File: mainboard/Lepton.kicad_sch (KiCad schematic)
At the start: 17 parts, among them IC1001 TXB0104RUT, IC1002 PCA9306JK, IC1003 TXB0104RUT, X1001 LEPTON, Y1001 25 MHz

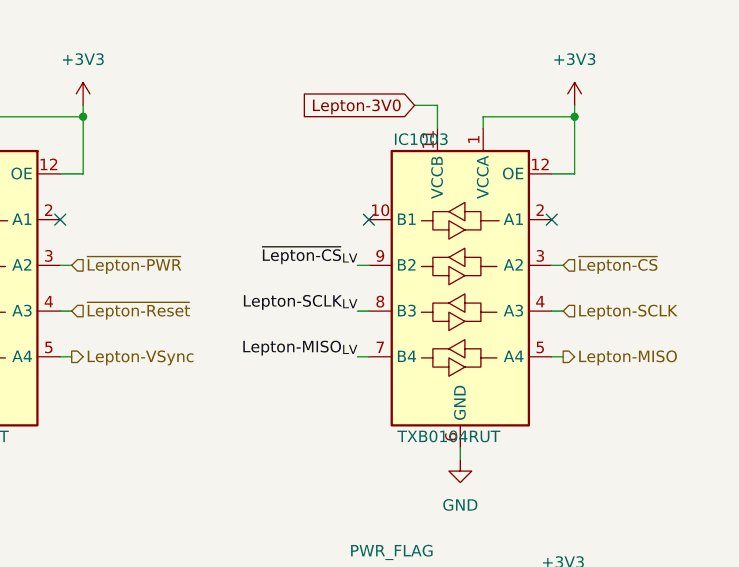
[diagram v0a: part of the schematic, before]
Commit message: Continue routing, add flash LEDs for the RGB camera, add PWM controller for the Display Backlight and the flash LEDs, add Polyfuse for the battery
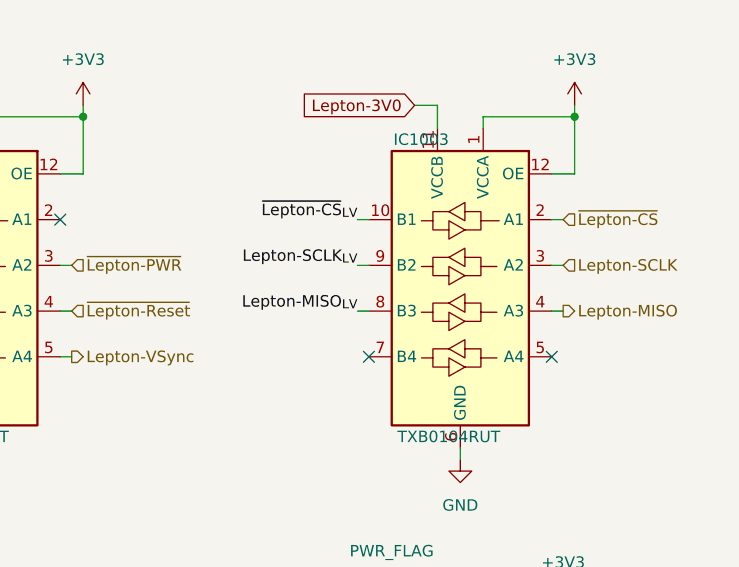
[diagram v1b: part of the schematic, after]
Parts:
- R1004, R1005, R1007, R1008: mouser# (none) -> 603-RC0603FR-073K3L
- R1006: mouser# (none) -> 603-RC0603FR-07200KL
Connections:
- net Lepton-MISO: now also IC1003.4 (A3); no longer IC1003.5 (A4)
- net Lepton-MISO_{LV}: now also IC1003.8 (B3); no longer IC1003.7 (B4)
- net Lepton-SCLK: now also IC1003.3 (A2); no longer IC1003.4 (A3)
- net Lepton-SCLK_{LV}: now also IC1003.9 (B2); no longer IC1003.8 (B3)
- net ~{Lepton-CS}: now also IC1003.2 (A1); no longer IC1003.3 (A2)
- net ~{Lepton-CS}_{LV}: now also IC1003.10 (B1); no longer IC1003.9 (B2)
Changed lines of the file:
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@@
 	)
 	(no_connect
+		(at 245.11 81.28)
+	)
+	(no_connect
 		(at 72.39 83.82)
 	)
 	(no_connect
-		(at 72.39 68.58)
+		(at 265.43 81.28)
 	)
 	(no_connect
-		(at 190.5 66.04)
+		(at 72.39 68.58)
 	)
 	(no_connect
-		(at 265.43 66.04)
+		(at 190.5 66.04)
 	)
 	(no_connect
@@
 		(at 85.09 50.8)
 	)
-	(no_connect
-		(at 245.11 66.04)
-	)
 	(wire
 		(pts
@@
 	(wire
 		(pts
-			(xy 265.43 81.28) (xy 266.7 81.28)
-		)
-		(stroke
-			(width 0)
-			(type default)
-		)
-	)
-	(wire
-		(pts
 			(xy 267.97 60.96) (xy 265.43 60.96)
 		)
@@
 	(wire
 		(pts
+			(xy 265.43 66.04) (xy 266.7 66.04)
+		)
+		(stroke
+			(width 0)
+			(type default)
+		)
+	)
+	(wire
+		(pts
 			(xy 203.2 54.61) (xy 203.2 55.88)
 		)
@@
 	(wire
 		(pts
-			(xy 96.52 76.2) (xy 85.09 76.2)
+			(xy 243.84 66.04) (xy 245.11 66.04)
 		)
 		(stroke
@@
 	(wire
 		(pts
-			(xy 242.57 121.92) (xy 245.11 121.92)
+			(xy 96.52 76.2) (xy 85.09 76.2)
 		)
 		(stroke
@@
 	(wire
 		(pts
-			(xy 71.12 81.28) (xy 71.12 88.9)
+			(xy 242.57 121.92) (xy 245.11 121.92)
 		)
 		(stroke
@@
 	(wire
 		(pts
-			(xy 265.43 137.16) (xy 271.78 137.16)
+			(xy 71.12 81.28) (xy 71.12 88.9)
 		)
 		(stroke
@@
 	(wire
 		(pts
-			(xy 85.09 53.34) (xy 86.36 53.34)
+			(xy 265.43 137.16) (xy 271.78 137.16)
 		)
 		(stroke
@@
 	(wire
 		(pts
-			(xy 54.61 76.2) (xy 57.15 76.2)
+			(xy 85.09 53.34) (xy 86.36 53.34)
 		)
 		(stroke
@@
 	(wire
 		(pts
-			(xy 85.09 73.66) (xy 97.79 73.66)
+			(xy 54.61 76.2) (xy 57.15 76.2)
 		)
 		(stroke
@@
 	(wire
 		(pts
-			(xy 243.84 81.28) (xy 245.11 81.28)
+			(xy 85.09 73.66) (xy 97.79 73.66)
 		)
 		(stroke
@@
 	)
 	(label "~{Lepton-CS}_{LV}"
-		(at 243.84 71.12 180)
+		(at 243.84 66.04 180)
 		(effects
 			(font
@@
 	)
 	(label "Lepton-MISO_{LV}"
-		(at 243.84 81.28 180)
+		(at 243.84 76.2 180)
 		(effects
 			(font
@@
 	)
 	(label "Lepton-SCLK_{LV}"
-		(at 243.84 76.2 180)
+		(at 243.84 71.12 180)
 		(effects
 			(font
@@
 	(hierarchical_label "~{Lepton-CS}"
 		(shape input)
-		(at 266.7 71.12 0)
+		(at 266.7 66.04 0)
 		(effects
 			(font
@@
 	(hierarchical_label "Lepton-MISO"
 		(shape output)
-		(at 266.7 81.28 0)
+		(at 266.7 76.2 0)
 		(effects
 			(font
@@
 	(hierarchical_label "Lepton-SCLK"
 		(shape input)
-		(at 266.7 76.2 0)
+		(at 266.7 71.12 0)
 		(effects
 			(font
@@
 			)
 		)
-		(property "Datasheet" "~"
+		(property "Datasheet" "https://www.mouser.com/catalog/specsheets/YAGEO_PYu_RC_Group_51_RoHS_L_12.pdf"
 			(at 265.43 128.27 0)
 			(effects
@@
 			)
 		)
-		(property "mouser#" ""
+		(property "mouser#" "603-RC0603FR-073K3L"
 			(at 265.43 128.27 0)
 			(effects
@@
 			)
 		)
-		(property "Datasheet" "~"
+		(property "Datasheet" "https://www.mouser.com/catalog/specsheets/YAGEO_PYu_RC_Group_51_RoHS_L_12.pdf"
 			(at 257.81 114.3 0)
 			(effects
@@
 			)
 		)
-		(property "mouser#" ""
+		(property "mouser#" "603-RC0603FR-07200KL"
 			(at 257.81 114.3 0)
 			(effects
@@
 			)
 		)
-		(property "Datasheet" "~"
+		(property "Datasheet" "https://www.mouser.com/catalog/specsheets/YAGEO_PYu_RC_Group_51_RoHS_L_12.pdf"
 			(at 267.97 128.27 0)
 			(effects
@@
 			)
 		)
-		(property "mouser#" ""
+		(property "mouser#" "603-RC0603FR-073K3L"
 			(at 267.97 128.27 0)
 			(effects
@@
 			)
 		)
-		(property "Datasheet" "~"
+		(property "Datasheet" "https://www.mouser.com/catalog/specsheets/YAGEO_PYu_RC_Group_51_RoHS_L_12.pdf"
 			(at 213.36 128.27 0)
 			(effects
@@
 			)
 		)
-		(property "mouser#" ""
+		(property "mouser#" "603-RC0603FR-073K3L"
 			(at 213.36 128.27 0)
 			(effects
@@
 			)
 		)
-		(property "Datasheet" "~"
+		(property "Datasheet" "https://www.mouser.com/catalog/specsheets/YAGEO_PYu_RC_Group_51_RoHS_L_12.pdf"
 			(at 215.9 128.27 0)
 			(effects
@@
 			)
 		)
-		(property "mouser#" ""
+		(property "mouser#" "603-RC0603FR-073K3L"
 			(at 215.9 128.27 0)
 			(effects

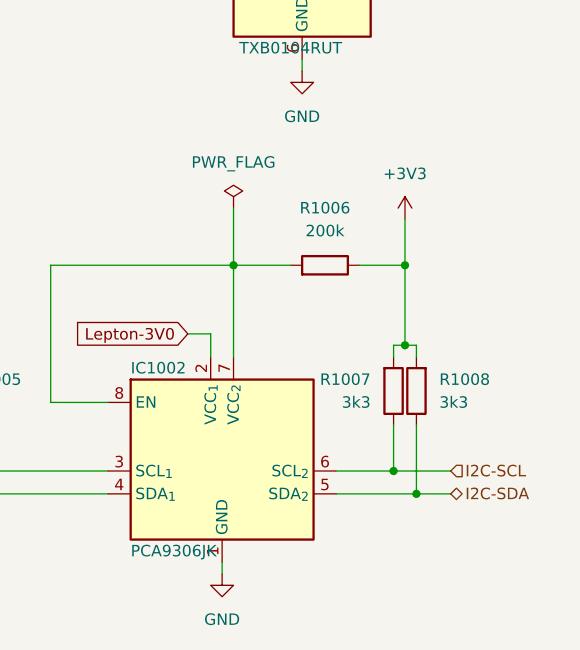
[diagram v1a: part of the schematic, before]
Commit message: New position for display connector
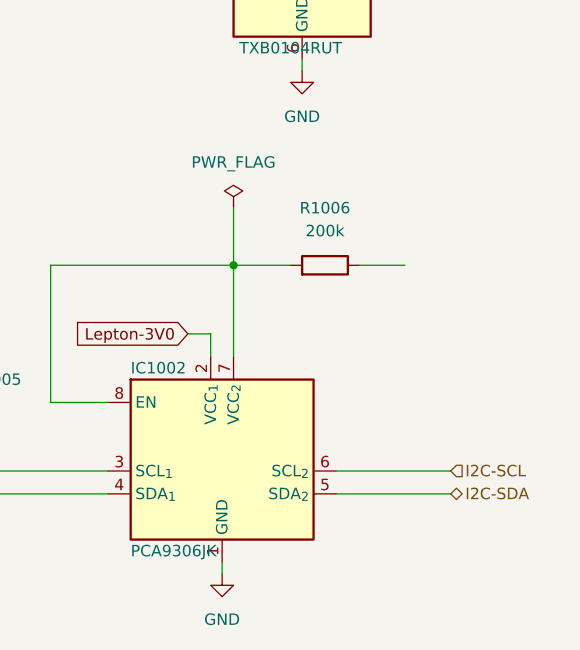
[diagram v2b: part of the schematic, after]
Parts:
- removed R1007, R1008: 3k3, Resistor_SMD:R_0603_1608Metric, symbol Device:R
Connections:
- net +3V3: no longer R1006.1

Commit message: Layout complete
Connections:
- net +3V3: now also R1006.1
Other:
- moved on the sheet: IC1001, IC1002, IC1003, R1001, R1002, R1004, R1005, R1006

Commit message: Task: Issue #7
- Increase the width of the cutout for the temperature sensor
- Add missing component informations
- Fix wrong component informations

Closes: #7

Signed-off-by: Daniel Kampert <DanielKampert@kampis-elektroecke.de>
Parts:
- R1002: mouser# 652-CR0603-J/-000ELF -> 652-CR1206-J/-000ELF
- R1006: manf# RC0603FR-07200KL -> RC0603FR-073K3L
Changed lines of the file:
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@@
 			)
 		)
-		(property "manf#" "RC0603FR-07200KL"
+		(property "manf#" "RC0603FR-073K3L"
 			(at 243.84 102.87 0)
 			(effects
@@
 			)
 		)
-		(property "mouser#" "652-CR0603-J/-000ELF"
+		(property "mouser#" "652-CR1206-J/-000ELF"
 			(at 66.04 82.55 0)
 			(effects

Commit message: Bug: Fixing several component issues
Closes: #17
Closes: #16
Closes: #15
Closes: #14
Closes: #13
Closes: #12

Signed-off-by: Daniel Kampert <danielkampert@kampis-elektroecke.de>
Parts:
- Y1001: manf ASDDV-25.000MHz-LC-T3 -> ABRACON; manf# ABRACON -> ASDDV-25.000MHz-LC-T3
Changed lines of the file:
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@@
 			)
 		)
-		(property "manf" "ASDDV-25.000MHz-LC-T3"
+		(property "manf" "ABRACON"
 			(at 105.41 129.54 0)
 			(effects
@@
 			)
 		)
-		(property "manf#" "ABRACON"
+		(property "manf#" "ASDDV-25.000MHz-LC-T3"
 			(at 105.41 129.54 0)
 			(effects

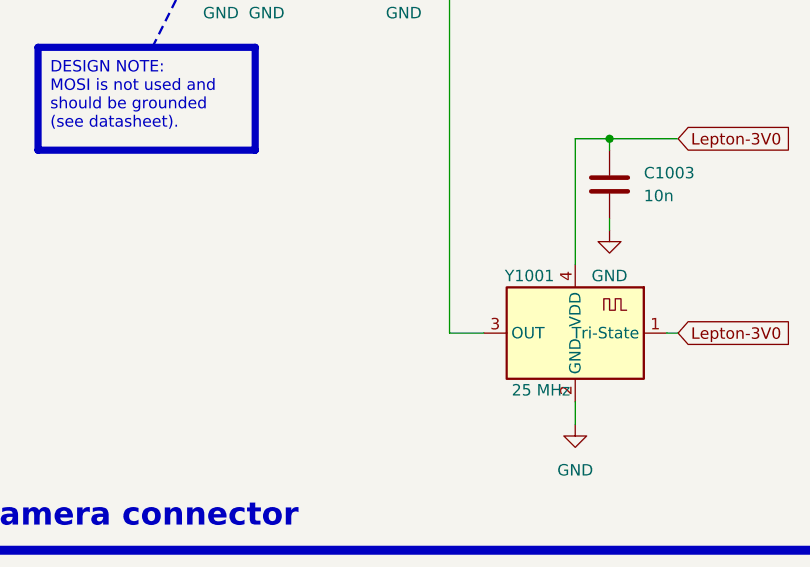
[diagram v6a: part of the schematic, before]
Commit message: Changed: Fix different minor assembly ToDos
Signed-off-by: Daniel Kampert <DanielKampert@kampis-elektroecke.de>
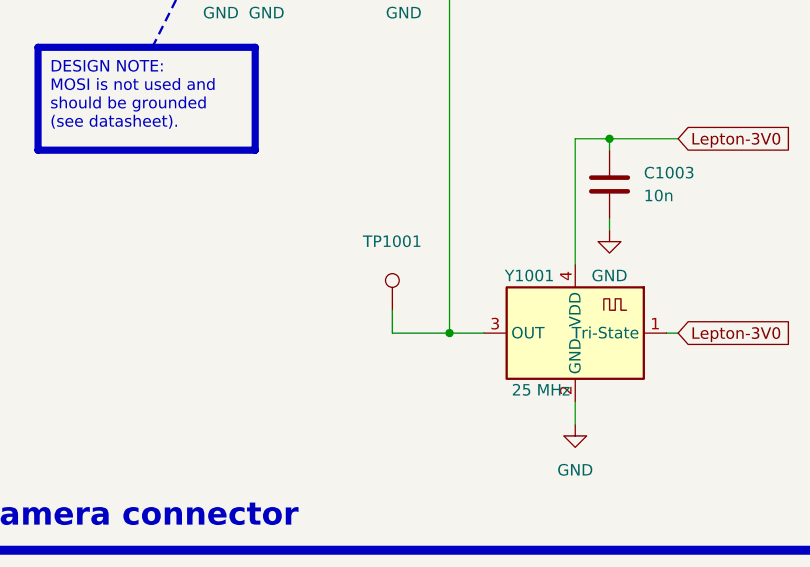
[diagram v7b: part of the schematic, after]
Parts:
- added TP1001: ~, Testpoints_Kampi:TestPoint_Pad_1.0x1.0mm, symbol Connector:TestPoint
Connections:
- net at X1001.26 (Pin_26), Y1001.3 (OUT): now also TP1001.1
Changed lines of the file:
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@@
 	)
 	(junction
+		(at 91.44 129.54)
+		(diameter 0)
+		(color 0 0 0 0)
+	)
+	(junction
 		(at 86.36 83.82)
 		(diameter 0)
@@
 	(wire
 		(pts
+			(xy 85.09 129.54) (xy 91.44 129.54)
+		)
+		(stroke
+			(width 0)
+			(type default)
+		)
+	)
+	(wire
+		(pts
 			(xy 71.12 66.04) (xy 72.39 66.04)
 		)
@@
 	(wire
 		(pts
-			(xy 247.65 102.87) (xy 252.73 102.87)
+			(xy 69.85 35.56) (xy 69.85 55.88)
 		)
 		(stroke
@@
 	(wire
 		(pts
-			(xy 69.85 35.56) (xy 69.85 55.88)
+			(xy 209.55 102.87) (xy 209.55 118.11)
 		)
 		(stroke
@@
 	(wire
 		(pts
-			(xy 209.55 102.87) (xy 209.55 118.11)
+			(xy 208.28 41.91) (xy 208.28 43.18)
 		)
 		(stroke
@@
 	(wire
 		(pts
-			(xy 208.28 41.91) (xy 208.28 43.18)
+			(xy 195.58 111.76) (xy 196.85 111.76)
 		)
 		(stroke
@@
 	(wire
 		(pts
-			(xy 195.58 111.76) (xy 196.85 111.76)
+			(xy 86.36 71.12) (xy 86.36 83.82)
 		)
 		(stroke
@@
 	(wire
 		(pts
-			(xy 86.36 71.12) (xy 86.36 83.82)
+			(xy 238.76 54.61) (xy 240.03 54.61)
 		)
 		(stroke
@@
 	(wire
 		(pts
-			(xy 238.76 54.61) (xy 240.03 54.61)
+			(xy 96.52 76.2) (xy 85.09 76.2)
 		)
 		(stroke
@@
 	(wire
 		(pts
-			(xy 96.52 76.2) (xy 85.09 76.2)
+			(xy 247.65 102.87) (xy 252.73 102.87)
 		)
 		(stroke
@@
 	(wire
 		(pts
+			(xy 85.09 127) (xy 85.09 129.54)
+		)
+		(stroke
+			(width 0)
+			(type default)
+		)
+	)
+	(wire
+		(pts
 			(xy 85.09 53.34) (xy 86.36 53.34)
 		)
@@
 					(unit 1)
 				)
+			)
+		)
+	)
+	(symbol
+		(lib_id "Connector:TestPoint")
+		(at 85.09 127 0)
+		(unit 1)
+		(exclude_from_sim no)
+		(in_bom no)
+		(on_board yes)
+		(dnp no)
+		(property "Reference" "TP1001"
+			(at 85.09 119.38 0)
+			(effects
+				(font
+					(size 1.27 1.27)
+				)
+			)
+		)
+		(property "Value" "~"
+			(at 85.09 121.285 0)
+			(effects
+				(font
+					(size 1.27 1.27)
+				)
+			)
+		)
+		(property "Footprint" "Testpoints_Kampi:TestPoint_Pad_1.0x1.0mm"
+			(at 90.17 127 0)
+			(effects
+				(font
+					(size 1.27 1.27)
+				)
+				(hide yes)
+			)
+		)
+		(property "Datasheet" "~"
+			(at 90.17 127 0)
+			(effects
+				(font
+					(size 1.27 1.27)
+				)
+				(hide yes)
+			)
+		)
+		(property "Description" "test point"
+			(at 85.09 127 0)
+			(effects
+				(font
+					(size 1.27 1.27)
+				)
+				(hide yes)
+			)
+		)
+		(property "manf" ""
+			(at 85.09 127 0)
+			(effects
+				(font
+					(size 1.27 1.27)
+				)
+				(hide yes)
+			)
+		)
+		(property "manf#" ""
+			(at 85.09 127 0)
+			(effects
+				(font
+					(size 1.27 1.27)
+				)
+				(hide yes)
+			)
+		)
+		(property "mouser#" ""
+			(at 85.09 127 0)
+			(effects
+				(font
+					(size 1.27 1.27)
+				)
+				(hide yes)
+			)
+		)
+		(property "CONFIG" ""
+			(at 85.09 127 0)
+			(effects
+				(font
+					(size 1.27 1.27)
+				)
+				(hide yes)
+			)
+		)
+		(pin "1"
+		)
+		(instances
+			(project "Mainboard"
+				(path "/d5742f03-3b1a-42e5-a384-018bd4b919aa/c5103ceb-5325-4a84-a025-9638a412984e/ffacc25a-000f-4387-8e2b-18f7ed663195"
+					(reference "TP1001")
+					(unit 1)
+				)

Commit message: Update to KiCad 10
Closes: #31, #29, #27

Signed-off-by: Daniel Kampert <DanielKampert@kampis-elektroecke.de>
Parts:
- TP1001: value ~ -> (none)
